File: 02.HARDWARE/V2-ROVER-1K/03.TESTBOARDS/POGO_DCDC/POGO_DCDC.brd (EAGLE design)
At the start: 39 x 64 mm, 13 parts, among them J1 FEMALE 2x3

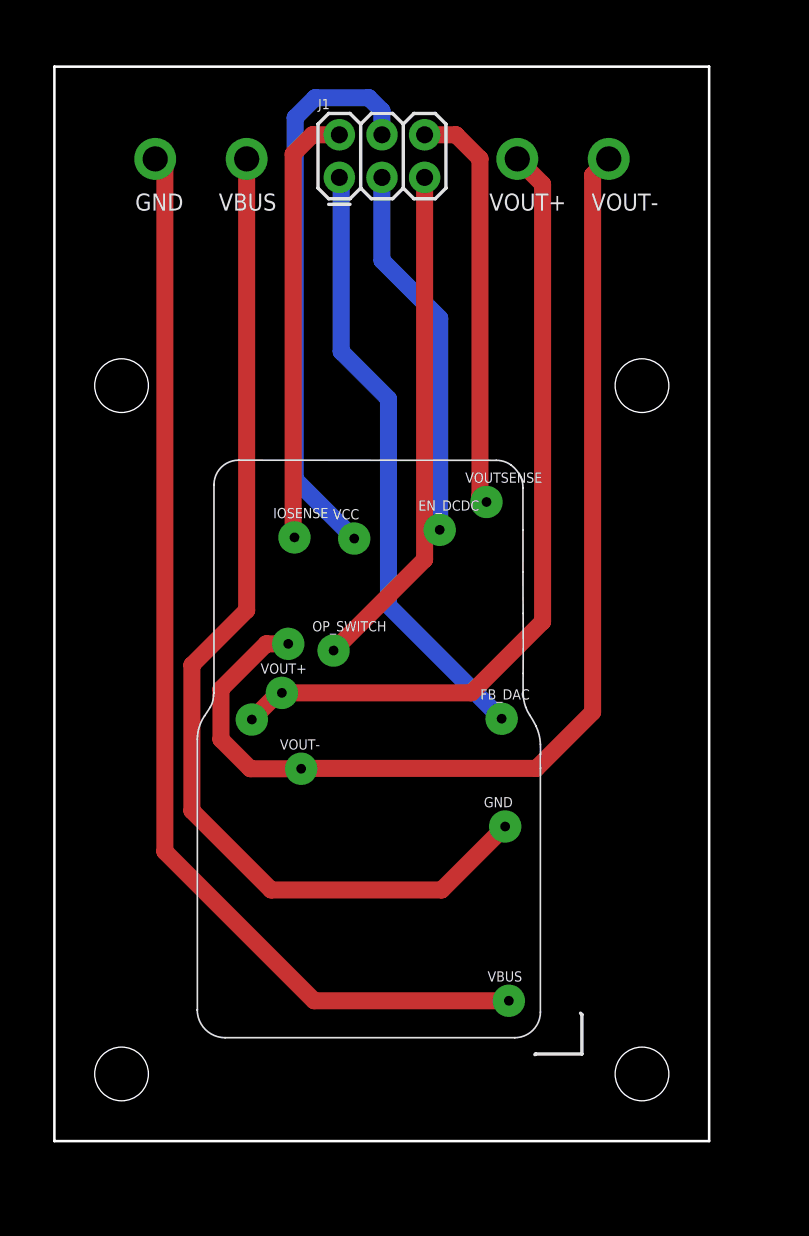
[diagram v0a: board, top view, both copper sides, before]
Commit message: TESTBOARDS Pedido PCBWAY 6ENERO
Revision antes de enviar a PCBWAY
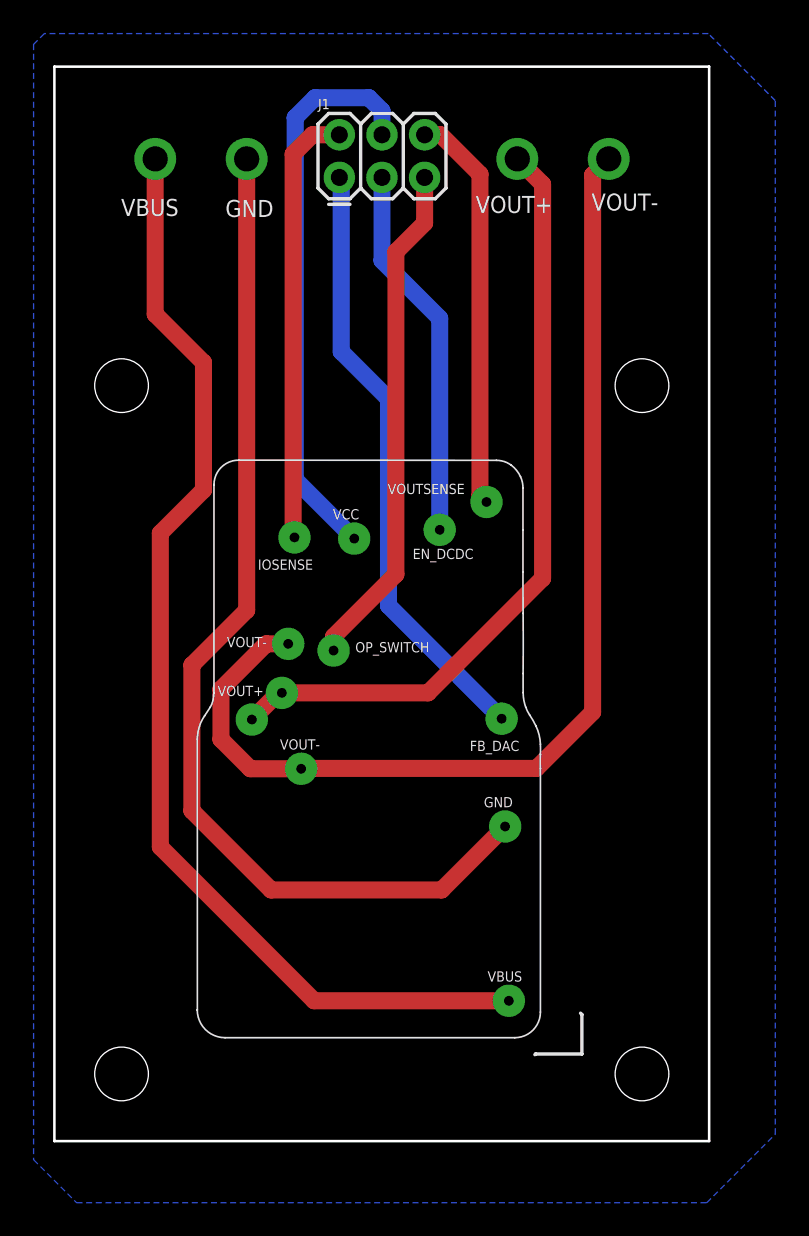
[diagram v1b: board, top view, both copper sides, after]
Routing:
- net VBUS: track 65.7 -> 67.8 mm
- net VOUT+: track 47.9 -> 46.4 mm
- net VOUTSENSE: track 24.5 -> 24.0 mm
- added copper zone on layer 16, net GND
